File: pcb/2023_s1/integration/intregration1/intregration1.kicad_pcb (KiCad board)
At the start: 2 copper layers, 36 parts, among them J1 Screw_Terminal_01x03, J2 Screw_Terminal_01x03, J4 Screw_Terminal_01x02, Q1 2N2219, Q2 2N2219, Q3 2N2219, Q4 2N2219, U2 NRF24L01_Breakout

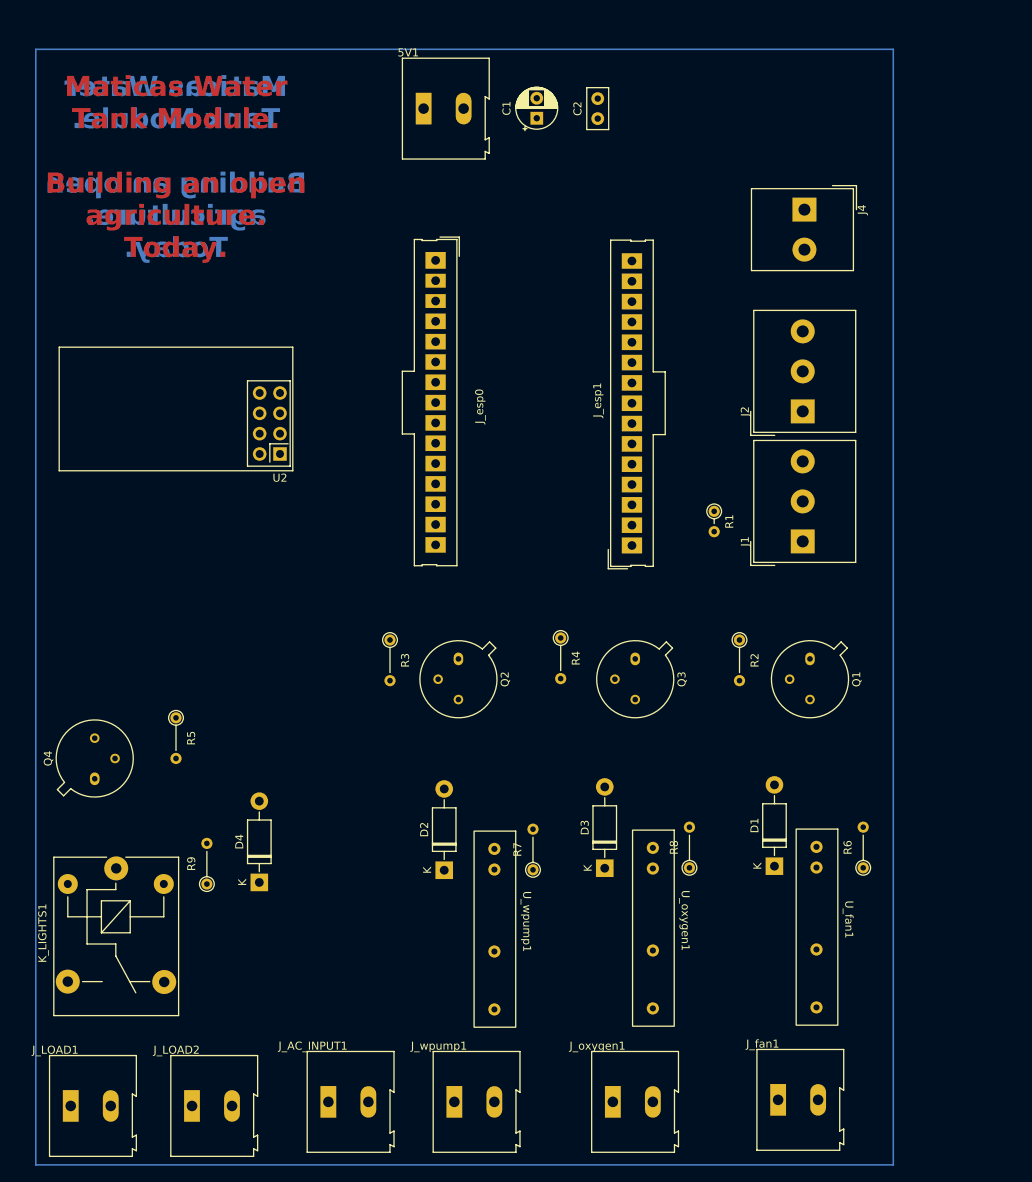
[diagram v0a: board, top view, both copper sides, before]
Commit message: update, routed the integration PCB, only production and testing is remaining
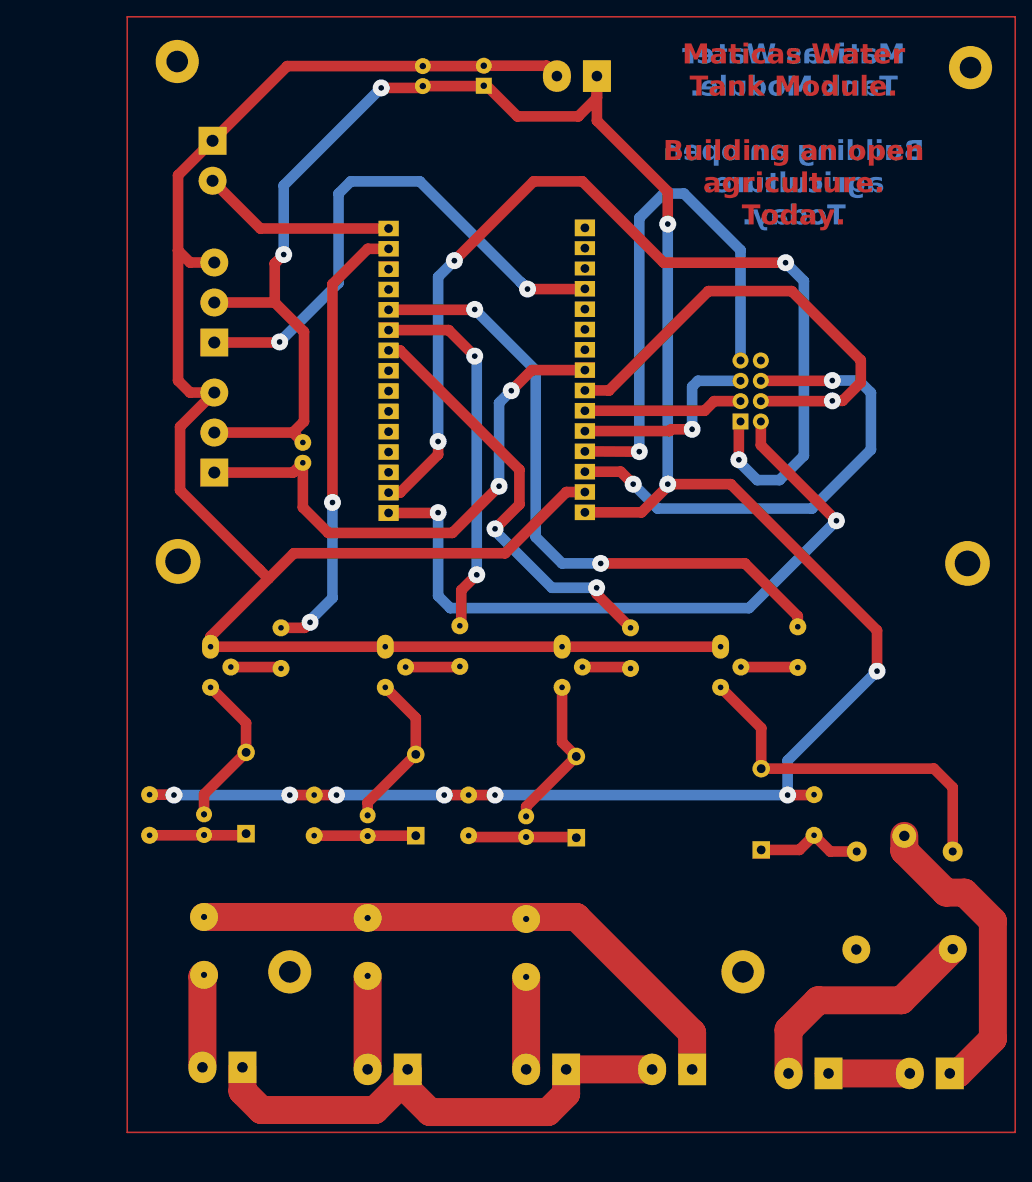
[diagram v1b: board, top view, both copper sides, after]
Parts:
- added H1: MountingHole, MountingHole:MountingHole_2.7mm_M2.5_Pad, B.Cu at (54.3, 33.5)
- added H2: MountingHole, MountingHole:MountingHole_2.7mm_M2.5_Pad, B.Cu at (153.4, 34.3)
- added H3: MountingHole, MountingHole:MountingHole_2.7mm_M2.5_Pad, B.Cu at (68.3, 147.3)
- added H4: MountingHole, MountingHole:MountingHole_2.7mm_M2.5_Pad, B.Cu at (125.0, 147.3)
- added H5: MountingHole, MountingHole:MountingHole_3.2mm_M3_DIN965_Pad, B.Cu at (153.0, 96.3)
- added H6: MountingHole, MountingHole:MountingHole_3.2mm_M3_DIN965_Pad, B.Cu at (54.4, 96.0)
- 5V1, C1, C2, D1, D2, D3, D4, J1, J2, J4, J_AC_INPUT1, J_LOAD1, J_LOAD2, J_esp0, J_esp1, J_fan1, J_oxygen1, J_wpump1, K_LIGHTS1, Q1, Q2, Q3, Q4, R1, R2, R3, R4, R5, R6, R7, R8, R9, U2, U_fan1, U_oxygen1, U_wpump1: moved to B.Cu
- moved J_LOAD1 110.0 mm to (150.8, 160.0), turned to 180 degrees
- moved K_LIGHTS1 98.6 mm to (145.1, 130.3)
- moved R6 89.3 mm to (50.8, 130.3)
- moved Q4 80.0 mm to (122.2, 106.7), turned to -90 degrees
- moved J_LOAD2 79.7 mm to (135.7, 160.0), turned to 180 degrees
- moved R5 78.6 mm to (131.8, 104.2)
- moved U_fan1 76.4 mm to (57.7, 136.7)
- moved R9 76.1 mm to (133.9, 130.3)
- moved Q1 74.9 mm to (58.4, 106.7)
- moved J4 74.5 mm to (58.7, 43.4)
- moved J1 74.1 mm to (58.9, 84.9)
- moved J2 74.1 mm to (58.9, 68.7)
- moved J_fan1 67.1 mm to (62.4, 159.3), turned to 180 degrees
- moved D1 66.2 mm to (62.9, 130.0)
- moved D4 62.9 mm to (127.3, 132.1)
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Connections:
- J4 pad 2: D19 -> D23
- R2 pad 1: D33 -> D22
- R3 pad 1: D16 -> D18
- R4 pad 1: D17 -> D19
- R5 pad 1: D18 -> D21
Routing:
- net 5v: track 0.00 -> 310.7 mm, vias 0 -> 11
- net GND5V: track 0.00 -> 238.4 mm
- net GND2: track 0.00 -> 123.5 mm, vias 0 -> 4
- net 3V3: track 0.00 -> 87.9 mm, vias 0 -> 2
- net D21: track 0.00 -> 80.6 mm, vias 0 -> 2
- net AC1: track 0.00 -> 71.6 mm
- net D25: track 0.00 -> 68.3 mm, vias 0 -> 2
- net D34: track 0.00 -> 68.1 mm, vias 0 -> 2
- net D12: track 0.00 -> 66.7 mm, vias 0 -> 1
- net AC2: track 0.00 -> 65.5 mm
- net D13: track 0.00 -> 62.2 mm, vias 0 -> 2
- net D26: track 0.00 -> 59.5 mm, vias 0 -> 1
- net D22: track 0.00 -> 56.4 mm, vias 0 -> 2
- net D18: track 0.00 -> 53.8 mm, vias 0 -> 2
- net D19: track 0.00 -> 46.8 mm, vias 0 -> 2
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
